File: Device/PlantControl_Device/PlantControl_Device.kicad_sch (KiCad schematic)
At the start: 14 parts, among them J2 Power, U1 NRF24L01_Breakout, U2 PIC18F15Q41-I/SS, U3 AHT20, U4 BH1750FVI-TR, U5 NCP1117-3.3Vout-20Vin

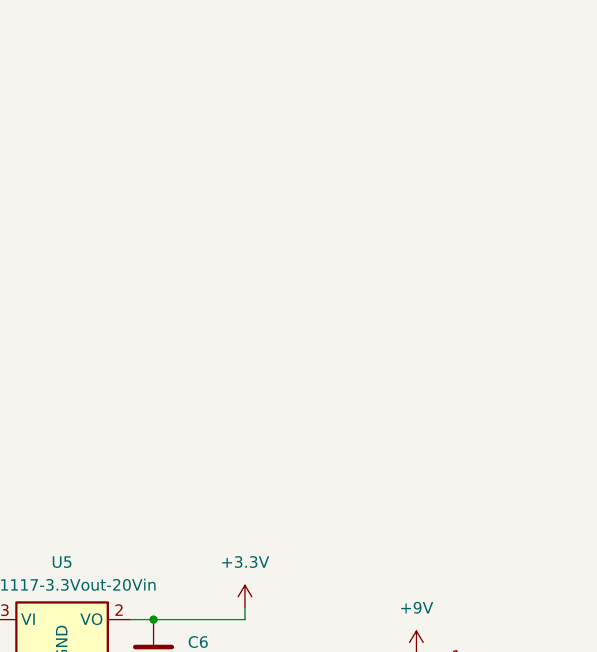
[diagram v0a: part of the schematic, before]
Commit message: Added PowerGood LEDs for 9V and 3.3V
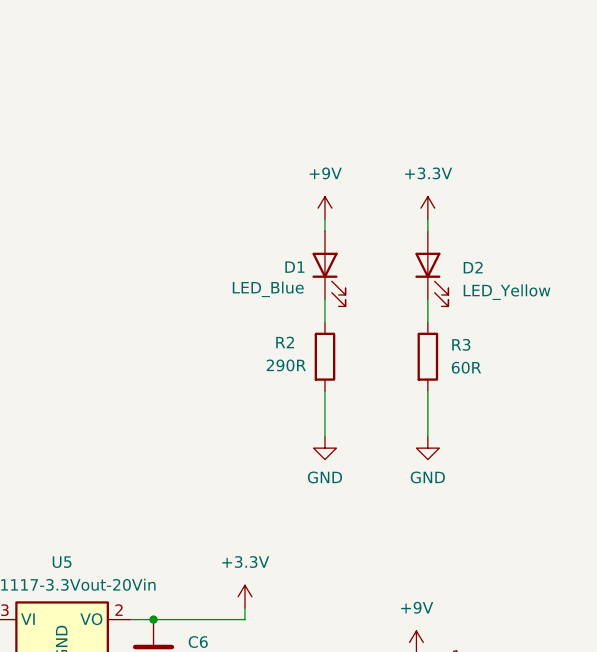
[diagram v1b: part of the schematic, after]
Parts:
- added D1: LED_Blue, LED_SMD:LED_0805_2012Metric_Pad1.15x1.40mm_HandSolder, symbol Device:LED
- added D2: LED_Yellow, LED_SMD:LED_0805_2012Metric_Pad1.15x1.40mm_HandSolder, symbol Device:LED
- added R2: 290R, Resistor_SMD:R_0805_2012Metric_Pad1.20x1.40mm_HandSolder, symbol Device:R
- added R3: 60R, Resistor_SMD:R_0805_2012Metric_Pad1.20x1.40mm_HandSolder, symbol Device:R
- C1, C2, C3, C4, C5, C6, C7: footprint (none) -> Capacitor_SMD:C_0805_2012Metric_Pad1.18x1.45mm_HandSolder
- R1: footprint (none) -> Resistor_SMD:R_0805_2012Metric_Pad1.20x1.40mm_HandSolder
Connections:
- net +3.3V: now also D2.2 (A)
- net +9V: now also D1.2 (A)
- net GND: now also R2.2, R3.2
- new net: D1.1 (K), R2.1
- new net: D2.1 (K), R3.1

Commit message: Added labels
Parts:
- added R4: 1kR, Resistor_SMD:R_0805_2012Metric_Pad1.20x1.40mm_HandSolder, symbol Device:R
- C4: now not fitted
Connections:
- net +3.3V: now also R4.1
- net SWCLK: now reaches U2.18 (RA1/ICSPCLK)
- net SWDIO: now reaches U2.19 (RA0/ICSPDAT)
- net nRST: now reaches U2.4 (*MCLR/VPP/RA3)
- net NRF_CE: now reaches U1.3 (CE)
- net SPI_nCS: now reaches U1.4 (~{CSN})
- net SPI_nCS: now also R4.2
- net SPI_SCK: now reaches U1.5 (SCK)
- net SPI_MOSI: now reaches U1.6 (MOSI)
- net SPI_MISO: now reaches U1.7 (MISO)
- net NRF_IRQ: now reaches U1.8 (IRQ)

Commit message: First layout
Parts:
- removed C7: 0.1uF, Capacitor_SMD:C_0805_2012Metric_Pad1.18x1.45mm_HandSolder, symbol Device:C
- added C8: 10uF, Capacitor_THT:C_Disc_D4.3mm_W1.9mm_P5.00mm, symbol Device:C
- added D3, D4, D5, D6, D7: LED_RGBA, cr_Library:cr_RGB_LED, symbol Device:LED_RGBA
- added J1: ADC1, Connector_PinHeader_2.00mm:PinHeader_1x03_P2.00mm_Vertical, symbol Connector_Generic:Conn_01x03
- added J3: ADC2, Connector_PinHeader_2.00mm:PinHeader_1x03_P2.00mm_Vertical, symbol Connector_Generic:Conn_01x03
- added J5: Conn_ARM_SWD_TagConnect_TC2030-NL, Connector:Tag-Connect_TC2030-IDC-NL_2x03_P1.27mm_Vertical, symbol Connector:Conn_ARM_SWD_TagConnect_TC2030-NL
- added R10, R11, R12, R13, R14, R15, R16, R17, R18, R19, R5, R6, R7, R8, R9: R, Resistor_THT:R_Axial_DIN0207_L6.3mm_D2.5mm_P7.62mm_Horizontal, symbol Device:R
- added R20, R21: R, Resistor_SMD:R_0805_2012Metric_Pad1.20x1.40mm_HandSolder, symbol Device:R
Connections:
- net +3.3V: now also C8.2, J1.1 (Pin_1), J3.1 (Pin_1), J5.1 (VCC), R20.1, R21.1
- net +9V: now also D3.4 (A), D4.4 (A), D5.4 (A), D6.4 (A), D7.4 (A)
- net GND: now also C8.1, J1.3 (Pin_3), J3.3 (Pin_3), J5.5 (GND)
- net I2C_SCL: now also U2.2 (RA5), R20.2
- net I2C_SDA: now also U2.3 (RA4), R21.2
- net SWCLK: now also J5.4 (SWCLK)
- net SWDIO: now also J5.2 (SWDIO)
- net nRST: now also J5.3 (~{RESET})
- net RGB2_B: now reaches U2.13 (RB4)
- net RGB2_B: now also R11.1, R12.1, R17.1, R5.1, R8.1
- net RGB2_G: now reaches U2.14 (RC2)
- net RGB2_G: now also R13.1, R14.1, R18.1, R6.1, R9.1
- net RGB2_R: now reaches U2.15 (RC1)
- net RGB2_R: now also R10.1, R15.1, R16.1, R19.1, R7.1
- new net: D5.1 (RK), R15.2
- new net: D5.2 (GK), R13.2
- new net: D5.3 (BK), R11.2
- new net: D4.1 (RK), R10.2
- new net: D4.2 (GK), R9.2
- new net: D4.3 (BK), R8.2
- new net: D6.1 (RK), R16.2
- new net: D6.2 (GK), R14.2
- new net: D6.3 (BK), R12.2
- new net: D7.1 (RK), R19.2
- new net: D7.2 (GK), R18.2
- new net: D7.3 (BK), R17.2
- new net: D3.1 (RK), R7.2
- new net: D3.2 (GK), R6.2
- new net: D3.3 (BK), R5.2
- new net Analog_In1: J1.2 (Pin_2)
- new net Analog_In2: J3.2 (Pin_2)
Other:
- moved on the sheet: C1, C2, C3, C4, C5, C6, D1, D2, J2, R1, R2, R3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
